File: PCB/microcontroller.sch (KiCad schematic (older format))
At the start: 0 parts

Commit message: PCB Edge.Cuts Defined
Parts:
- added U1: DEV_KIT_EK-TM4C123GXL, local:DEV_KIT_EK-TM4C123GXL, symbol DEV_KIT_EK-TM4C123GXL
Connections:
- new net 5V: U1.20 (5V)
- new net GND: U1.19 (GND), U1.40 (GND)
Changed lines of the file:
@@
 EELAYER 26 0
 EELAYER END
-$Descr A4 11693 8268
+$Descr A 11000 8500
 encoding utf-8
-Sheet 1 5
-Title ""
-Date ""
-Rev ""
-Comp ""
+Sheet 3 20
+Title "Christmas Tree Disco"
+Date "2017-08-01"
+Rev "01"
+Comp "www.GitHub.com/Cryochasm"
 Comment1 ""
 Comment2 ""
@@
 Comment4 ""
 $EndDescr
+$Comp
+L DEV_KIT_EK-TM4C123GXL U1
+U 1 1 59812138
+P 5300 4000
+F 0 "U1" H 5300 5187 50  0000 C CNN
+F 1 "DEV_KIT_EK-TM4C123GXL" H 5300 5081 50  0000 C CNN
+F 2 "local:DEV_KIT_EK-TM4C123GXL" V 5850 3000 60  0001 C CNN
+F 3 "http://www.ti.com/lit/ds/spms376e/spms376e.pdf" V 5850 3000 60  0001 C CNN
+F 4 "EK-TM4C123GXL" H 5300 4000 60  0001 C CNN "MPN"
+F 5 "Development Boards & Kits - ARM TIVA LaunchPAD" H 5300 4000 60  0001 C CNN "Description"
+F 6 "No" H 5300 4000 60  0001 C CNN "Included in BOM"
+	1    5300 4000
+	1    0    0    -1
+$EndComp
+Text HLabel 1300 7500 0    50   Input ~ 0
+~~POWER[0..1]
+Wire Bus Line
+	1300 7500 1400 7500
+Wire Bus Line
+	1400 7500 1400 7700
+Entry Wire Line
+	1400 7600 1500 7700
+Entry Wire Line
+	1400 7700 1500 7800
+Wire Wire Line
+	1500 7700 1900 7700
+Wire Wire Line
+	1500 7800 1900 7800
+Text Label 1900 7800 0    50   ~ 0
+5V
+Text Label 1900 7700 0    50   ~ 0
+GND
+Text Label 1500 7700 0    50   ~ 0
+~~POWER0
+Text Label 1500 7800 0    50   ~ 0
+~~POWER1
+Text HLabel 1300 6900 0    50   BiDi ~ 0
+~~SHIFT_CTRL[0..4]
+Wire Bus Line
+	1300 6900 1400 6900
+Wire Bus Line
+	1400 6900 1400 7300
+Entry Wire Line
+	1400 6900 1500 7000
+Entry Wire Line
+	1400 7000 1500 7100
+Entry Wire Line
+	1400 7100 1500 7200
+Entry Wire Line
+	1400 7200 1500 7300
+Entry Wire Line
+	1400 7300 1500 7400
+Wire Wire Line
+	1500 7000 2100 7000
+Wire Wire Line
+	1500 7100 2100 7100
+Wire Wire Line
+	1500 7200 2100 7200
+Wire Wire Line
+	1500 7300 2100 7300
+Wire Wire Line
+	1500 7400 2100 7400
+Text Label 2100 7000 0    50   ~ 0
+DATA
+Text Label 2100 7100 0    50   ~ 0
+SCLK
+Text Label 2100 7200 0    50   ~ 0
+LAT
+Text Label 2100 7300 0    50   ~ 0
+GSCLK
+Text Label 2100 7400 0    50   ~ 0
+ERROR_RD
+Text Label 1500 7000 0    50   ~ 0
+~~SHIFT_CTRL0
+Text Label 1500 7100 0    50   ~ 0
+~~SHIFT_CTRL1
+Text Label 1500 7200 0    50   ~ 0
+~~SHIFT_CTRL2
+Text Label 1500 7300 0    50   ~ 0
+~~SHIFT_CTRL3
+Text Label 1500 7400 0    50   ~ 0
+~~SHIFT_CTRL4
+Text Label 7200 3600 0    50   ~ 0
+GND
+Text Label 5200 5000 3    50   ~ 0
+5V
+Wire Wire Line
+	5200 4800 5200 5000
+Wire Wire Line
+	5100 4800 5100 5000
+Wire Wire Line
+	7000 3600 7200 3600
+Text Label 5100 5000 3    50   ~ 0
+GND
 $EndSCHEMATC

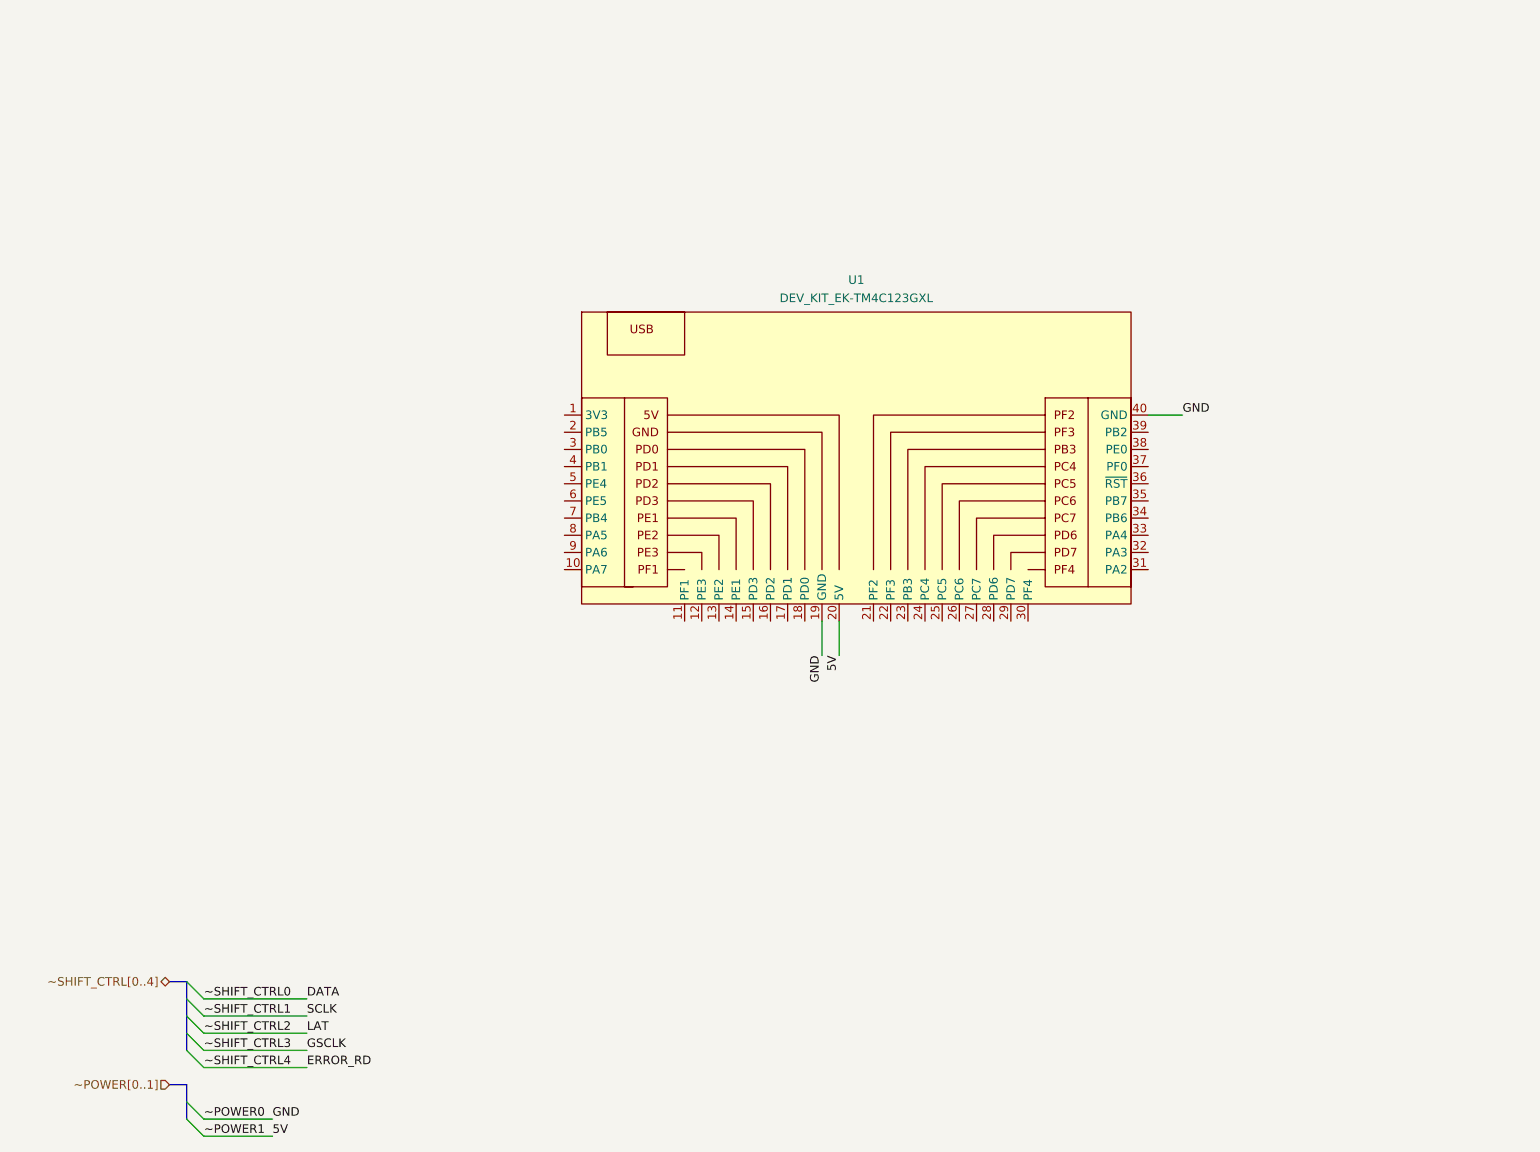
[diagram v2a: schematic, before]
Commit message: Added Logic Level Conversion
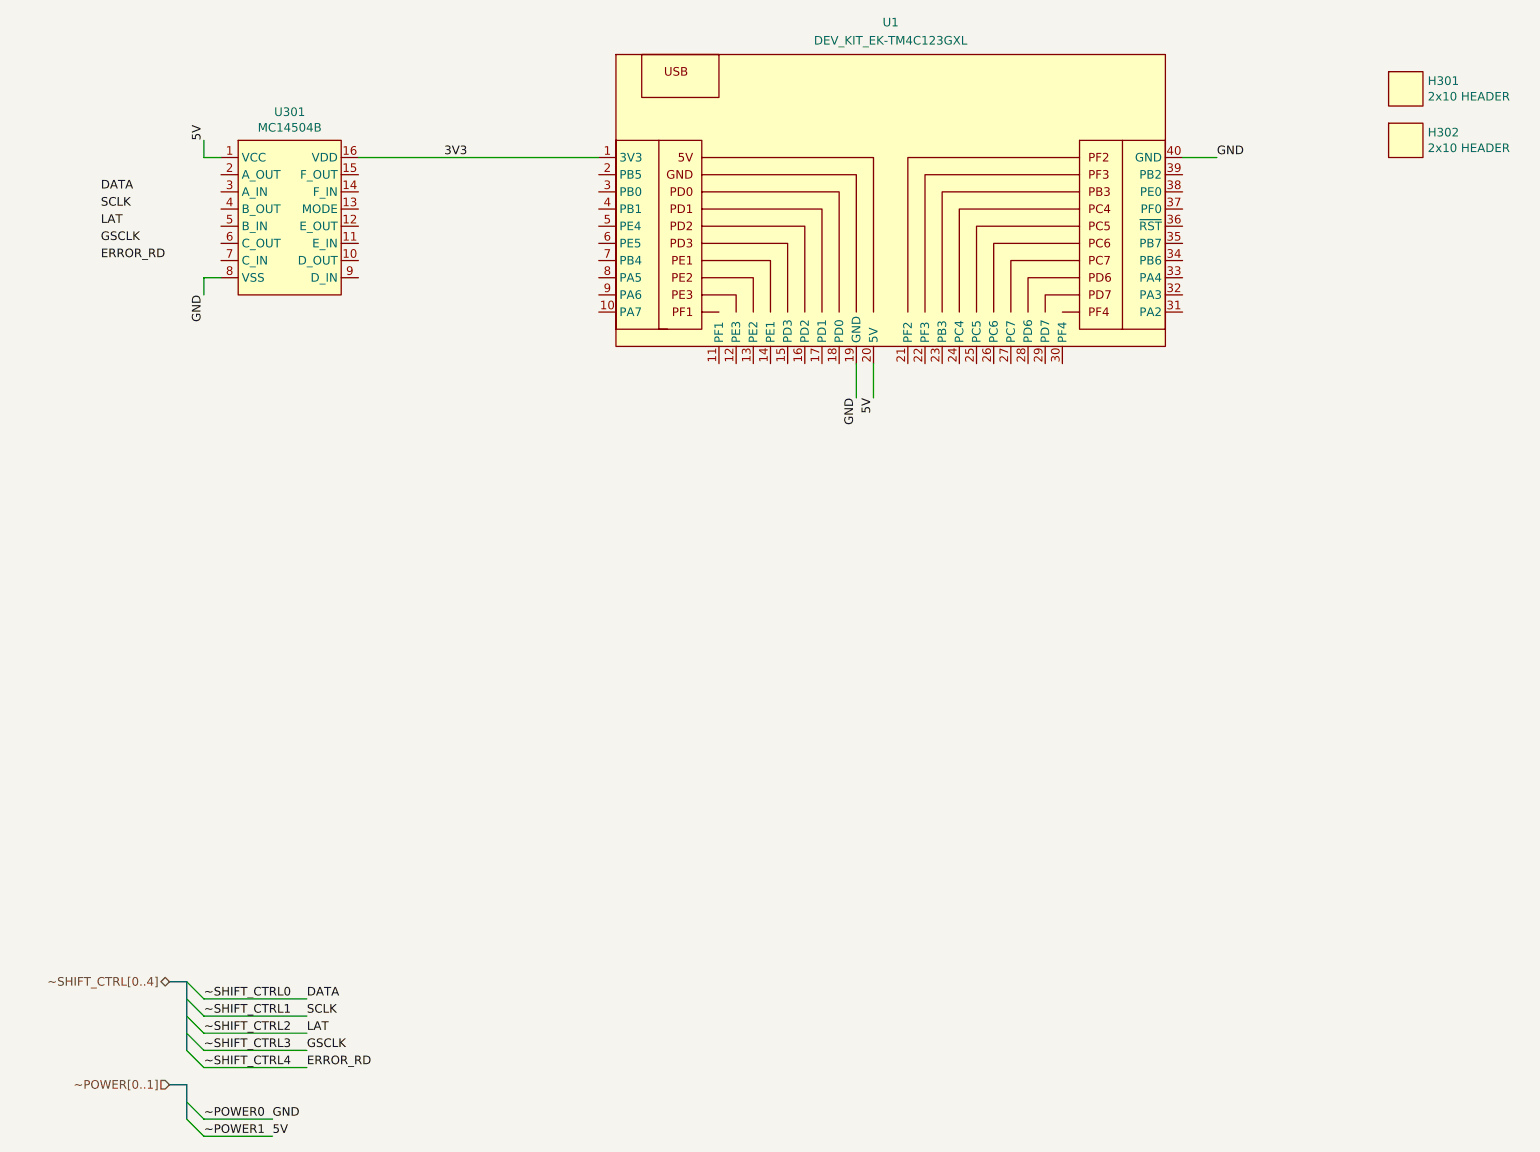
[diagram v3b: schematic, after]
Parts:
- added H301, H302: 2x10 HEADER, local:2x10_header_3d, symbol Generic
- added U301: MC14504B, local:SOIC-16, symbol MC14504B
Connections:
- net 5V: now also U301.1 (VCC)
- net GND: now also U301.8 (VSS)
- net 3V3: now reaches U1.1 (3V3)
- net 3V3: now also U301.16 (VDD)
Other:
- moved on the sheet: U1
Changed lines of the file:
@@
 $Descr A 11000 8500
 encoding utf-8
-Sheet 3 19
+Sheet 3 20
 Title "Christmas Tree Disco"
 Date "2017-08-01"
@@
 L DEV_KIT_EK-TM4C123GXL U1
 U 1 1 59812138
-P 5300 4000
-F 0 "U1" H 5300 5187 50  0000 C CNN
-F 1 "DEV_KIT_EK-TM4C123GXL" H 5300 5081 50  0000 C CNN
-F 2 "local:DEV_KIT_EK-TM4C123GXL" V 5850 3000 60  0001 C CNN
-F 3 "http://www.ti.com/lit/ds/spms376e/spms376e.pdf" V 5850 3000 60  0001 C CNN
-F 4 "EK-TM4C123GXL" H 5300 4000 60  0001 C CNN "MPN"
-F 5 "Development Boards & Kits - ARM TIVA LaunchPAD" H 5300 4000 60  0001 C CNN "Description"
-F 6 "No" H 5300 4000 60  0001 C CNN "Included in BOM"
-	1    5300 4000
+P 5500 2500
+F 0 "U1" H 5500 3687 50  0000 C CNN
+F 1 "DEV_KIT_EK-TM4C123GXL" H 5500 3581 50  0000 C CNN
+F 2 "local:DEV_KIT_EK-TM4C123GXL" V 6050 1500 60  0001 C CNN
+F 3 "http://www.ti.com/lit/ds/spms376e/spms376e.pdf" V 6050 1500 60  0001 C CNN
+F 4 "EK-TM4C123GXL" H 5500 2500 60  0001 C CNN "MPN"
+F 5 "Development Boards & Kits - ARM TIVA LaunchPAD" H 5500 2500 60  0001 C CNN "Description"
+F 6 "No" H 5500 2500 60  0001 C CNN "Included in BOM"
+	1    5500 2500
 	1    0    0    -1
 $EndComp
@@
 Text Label 1500 7400 0    50   ~ 0
 ~~SHIFT_CTRL4
-Text Label 7200 3600 0    50   ~ 0
+Text Label 7400 2100 0    50   ~ 0
 GND
-Text Label 5200 5000 3    50   ~ 0
+Text Label 5400 3500 3    50   ~ 0
 5V
 Wire Wire Line
-	5200 4800 5200 5000
+	5400 3300 5400 3500
 Wire Wire Line
-	5100 4800 5100 5000
+	5300 3300 5300 3500
 Wire Wire Line
-	7000 3600 7200 3600
-Text Label 5100 5000 3    50   ~ 0
+	7200 2100 7400 2100
+Text Label 5300 3500 3    50   ~ 0
+GND
+$Comp
+L Generic H301
+U 1 1 5984BC75
+P 8500 1700
+F 0 "H301" H 8628 1746 50  0000 L CNN
+F 1 "2x10 HEADER" H 8628 1655 50  0000 L CNN
+F 2 "local:2x10_header_3d" H 8500 1500 50  0001 C CNN
+F 3 "http://www.molex.com/pdm_docs/sd/015912200_sd.pdf" H 8500 1700 50  0001 C CNN
+F 4 "0015912200" H 8500 1400 50  0001 C CNN "MPN"
+F 5 "20 Positions Header, Breakaway Connector 0.100\" (2.54mm) Surface Mount Tin" H 8500 1300 50  0001 C CNN "Description"
+F 6 "Yes" H 8500 1200 50  0001 C CNN "Included in BOM"
+	1    8500 1700
+	1    0    0    -1
+$EndComp
+$Comp
+L Generic H302
+U 1 1 5984BD4E
+P 8500 2000
+F 0 "H302" H 8628 2046 50  0000 L CNN
+F 1 "2x10 HEADER" H 8628 1955 50  0000 L CNN
+F 2 "local:2x10_header_3d" H 8500 1800 50  0001 C CNN
+F 3 "http://www.molex.com/pdm_docs/sd/015912200_sd.pdf" H 8500 2000 50  0001 C CNN
+F 4 "0015912200" H 8500 1700 50  0001 C CNN "MPN"
+F 5 "20 Positions Header, Breakaway Connector 0.100\" (2.54mm) Surface Mount Tin" H 8500 1600 50  0001 C CNN "Description"
+F 6 "Yes" H 8500 1500 50  0001 C CNN "Included in BOM"
+	1    8500 2000
+	1    0    0    -1
+$EndComp
+$Comp
+L MC14504B U301
+U 1 1 5984BDBB
+P 2000 2400
+F 0 "U301" H 2000 2965 50  0000 C CNN
+F 1 "MC14504B" H 2000 2874 50  0000 C CNN
+F 2 "local:SOIC-16" H 1900 2900 50  0001 C CNN
+F 3 "http://www.onsemi.com/pub/Collateral/MC14504B-D.PDF" H 2000 3100 50  0001 C CNN
+F 4 "MC14504B" H 2000 3400 50  0001 C CNN "MPN"
+F 5 "Voltage Level Translator Unidirectional Circuit 6 Channel 16-SOIC" H 2000 3200 50  0001 C CNN "Description"
+F 6 "Yes" H 2000 3300 50  0001 C CNN "Included in BOM"
+	1    2000 2400
+	1    0    0    -1
+$EndComp
+Wire Wire Line
+	3800 2100 2400 2100
+Text Label 2900 2100 0    50   ~ 0
+3V3
+Text Label 900  2300 0    50   ~ 0
+DATA
+Text Label 900  2400 0    50   ~ 0
+SCLK
+Text Label 900  2500 0    50   ~ 0
+LAT
+Text Label 900  2600 0    50   ~ 0
+GSCLK
+Text Label 900  2700 0    50   ~ 0
+ERROR_RD
+Wire Wire Line
+	1600 2100 1500 2100
+Wire Wire Line
+	1500 2100 1500 2000
+Text Label 1500 2000 1    50   ~ 0
+5V
+Wire Wire Line
+	1600 2800 1500 2800
+Wire Wire Line
+	1500 2800 1500 2900
+Text Label 1500 2900 3    50   ~ 0
 GND
 $EndSCHEMATC

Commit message: Preliminary PCB layout
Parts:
- added C18, C19: Capacitor, local:SMD-0805, symbol Capacitor
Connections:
- net 3V3: now also C19.2
- net 5V: now also C18.1
- net DATA: now also U301.2 (A_OUT)
- net ERROR_RD: now also U301.11 (E_IN)
- net GND: now also U301.13 (MODE), C18.2, C19.1
- net GSCLK: now also U301.10 (D_OUT)
- net LAT: now also U301.6 (C_OUT)
- net SCLK: now also U301.4 (B_OUT)
- net at U1.27 (PC7): now also U301.7 (C_IN)
- net at U1.28 (PD6): now also U301.5 (B_IN)
- net at U1.29 (PD7): now also U301.3 (A_IN)
- net at U1.30 (PF4): now also U301.9 (D_IN)
- net at U1.31 (PA2): now also U301.12 (E_OUT)
- no-connect marks 0 -> 33
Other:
- moved on the sheet: U301

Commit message: PCB Layout
TODO: Change pinouts on dev kit to be compatable with Capacitive Touch
Audio booster pack.
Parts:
- C18, C19: value Capacitor -> 0.1u; Description ? -> 0.1µF ±10% 25V Ceramic Capacitor X7R 0805 (2012 Metric); MPN ? -> CL21B104KACWPNC
- U301: MPN MC14504B -> MC14504BDG
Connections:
- net LAT_3V3: now reaches U1.27 (PC7), U301.7 (C_IN)
- net SCLK_3V3: now reaches U1.28 (PD6), U301.5 (B_IN)
- net DATA_3V3: now reaches U1.29 (PD7), U301.3 (A_IN)
- net GSCLK_3V3: now reaches U1.30 (PF4), U301.9 (D_IN)
- net ERROR_RD_3V3: now reaches U1.31 (PA2), U301.12 (E_OUT)
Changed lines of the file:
@@
 F 2 "local:SOIC-16" H 6200 5800 50  0001 C CNN
 F 3 "http://www.onsemi.com/pub/Collateral/MC14504B-D.PDF" H 6300 6000 50  0001 C CNN
-F 4 "MC14504B" H 6300 6300 50  0001 C CNN "MPN"
+F 4 "MC14504BDG" H 6300 6300 50  0001 C CNN "MPN"
 F 5 "Voltage Level Translator Unidirectional Circuit 6 Channel 16-SOIC" H 6300 6100 50  0001 C CNN "Description"
 F 6 "Yes" H 6300 6200 50  0001 C CNN "Included in BOM"
@@
 GND
 $Comp
+L Capacitor C18
+U 1 1 59876312
+P 6000 4600
+F 0 "C18" V 5954 4668 50  0000 L CNN
+F 1 "0.1u" V 6045 4668 50  0000 L CNN
+F 2 "local:SMD-0805" H 6000 4600 60  0001 C CNN
+F 3 "http://www.samsungsem.com/kr/support/library/product-catalog/mlcc.jsp" H 6000 4600 60  0001 C CNN
+F 4 "CL21B104KACWPNC" H 6000 4600 60  0001 C CNN "MPN"
+F 5 "0.1µF ±10% 25V Ceramic Capacitor X7R 0805 (2012 Metric)" H 6000 4600 60  0001 C CNN "Description"
+F 6 "Yes" H 6000 4600 60  0001 C CNN "Included in BOM"
+	1    6000 4600
+	1    0    0    -1
+$EndComp
+Wire Wire Line
+	5900 4600 5800 4600
+Connection ~ 5800 4600
+Wire Wire Line
+	6100 4600 6500 4600
+Wire Wire Line
+	6700 4600 6800 4600
+Connection ~ 6800 4600
+Wire Wire Line
+	6300 4600 6300 4500
+Connection ~ 6300 4600
+Text Label 6300 4500 1    50   ~ 0
+GND
+Text Label 6600 3400 0    50   ~ 0
+GSCLK_3V3
+Text Label 7400 3000 0    50   ~ 0
+ERROR_RD_3V3
+Text Label 6400 3500 3    50   ~ 0
+DATA_3V3
+Text Label 6300 3500 3    50   ~ 0
+SCLK_3V3
+Text Label 6200 3500 3    50   ~ 0
+LAT_3V3
+$Comp
 L Capacitor C19
-U 1 1 598762EF
+U 1 1 59890F4A
 P 6600 4600
 F 0 "C19" V 6554 4668 50  0000 L CNN
-F 1 "Capacitor" V 6645 4668 50  0000 L CNN
+F 1 "0.1u" V 6645 4668 50  0000 L CNN
 F 2 "local:SMD-0805" H 6600 4600 60  0001 C CNN
-F 3 "" H 6600 4600 60  0001 C CNN
-F 4 "?" H 6600 4600 60  0001 C CNN "MPN"
-F 5 "?" H 6600 4600 60  0001 C CNN "Description"
+F 3 "http://www.samsungsem.com/kr/support/library/product-catalog/mlcc.jsp" H 6600 4600 60  0001 C CNN
+F 4 "CL21B104KACWPNC" H 6600 4600 60  0001 C CNN "MPN"
+F 5 "0.1µF ±10% 25V Ceramic Capacitor X7R 0805 (2012 Metric)" H 6600 4600 60  0001 C CNN "Description"
 F 6 "Yes" H 6600 4600 60  0001 C CNN "Included in BOM"
 	1    6600 4600
 	1    0    0    -1
 $EndComp
-$Comp
-L Capacitor C18
-U 1 1 59876312
-P 6000 4600
-F 0 "C18" V 5954 4668 50  0000 L CNN
-F 1 "Capacitor" V 6045 4668 50  0000 L CNN
-F 2 "local:SMD-0805" H 6000 4600 60  0001 C CNN
-F 3 "" H 6000 4600 60  0001 C CNN
-F 4 "?" H 6000 4600 60  0001 C CNN "MPN"
-F 5 "?" H 6000 4600 60  0001 C CNN "Description"
-F 6 "Yes" H 6000 4600 60  0001 C CNN "Included in BOM"
-	1    6000 4600
-	1    0    0    -1
-$EndComp
-Wire Wire Line
-	5900 4600 5800 4600
-Connection ~ 5800 4600
-Wire Wire Line
-	6100 4600 6500 4600
-Wire Wire Line
-	6700 4600 6800 4600
-Connection ~ 6800 4600
-Wire Wire Line
-	6300 4600 6300 4500
-Connection ~ 6300 4600
-Text Label 6300 4500 1    50   ~ 0
-GND
 $EndSCHEMATC
